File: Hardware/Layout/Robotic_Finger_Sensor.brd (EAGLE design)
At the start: 14 x 15.2 mm, 11 parts, among them U1 VCNL4040

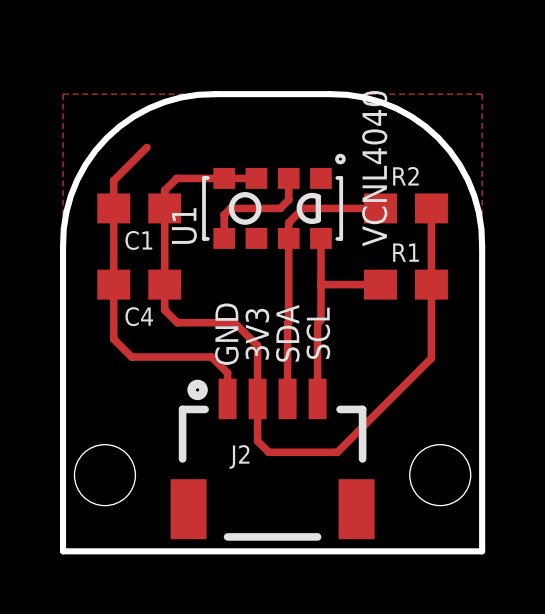
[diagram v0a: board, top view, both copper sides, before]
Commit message: Adding pressure sensor. Cleaning up repo.
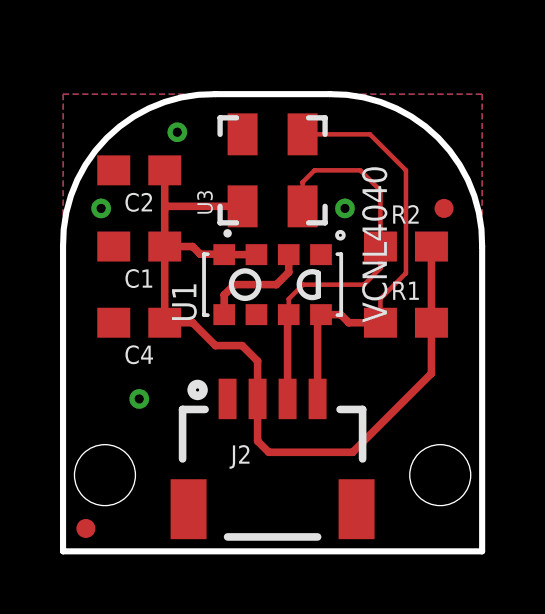
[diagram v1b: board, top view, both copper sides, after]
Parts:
- removed U$1: OSHW-LOGOS, SparkFun:OSHW-LOGO-S
- added C2: 0.1uF, SparkFun-Capacitors:0603
- added FD1, FD2: FIDUCIALUFIDUCIAL, SparkFun-Aesthetics:FIDUCIAL-MICRO
- added U$10: (no value), buzzard_labels:SENSOR5
- added U$11: (no value), Labels-0_04:(QWIIC)
- added U$5: (no value), buzzard_labels:ROBOTIC3
- added U$8: (no value), buzzard_labels:FINGER4
- added U3: MS5637, MS5637:MS5637
- moved U1 2.54 mm to (6.99, 8.89)
- moved C4 1.27 mm to (2.54, 7.62)
- moved R1 1.27 mm to (11.4, 7.62)
- moved C1 1.27 mm to (2.54, 10.2)
- moved R2 1.27 mm to (11.4, 10.2)
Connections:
- net 3.3V: now also C2.1, U3.1
- net GND: now also C2.2, U3.4
- net SCL: now also U3.3
- net SDA: now also U3.2
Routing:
- net GND: track 12.0 -> 0.00 mm, vias 0 -> 4
- net SCL: track 7.38 -> 14.3 mm
- net SDA: track 9.14 -> 13.3 mm
- net 3.3V: track 26.2 -> 29.4 mm
- added copper zone on layer 16, net GND
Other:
- board text removed: "3V3"
- board text removed: "GND"
- board text removed: "Robotic Finger Sensor"
- board text removed: "SCL"
- board text removed: "SDA"
